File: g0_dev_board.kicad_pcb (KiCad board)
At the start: 4 copper layers, 80 x 114 mm, 198 parts, among them J201 USB_B_Mini, J202 F103_SWD, J301 USB_B_Mini, J401 RJ45_Hanrun_HR911105A_Horizon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, J501 DM3AT-SF-PEJM5, J801 Uno_IOH, J802 Uno_IOL, J803 Uno_POWER, J804 Uno_ANALOG, J805 J_LA_L, J806 J_LA_R, Q201 MMBT3904, SW701 RESET, SW702 USER, U101 STM32G0B1CCT6, U201 USBLC6-2SC6, U202 AP7361C-33E, U203 STM32F103CBTx, U301 USBLC6-2SC6, U302 FT232RL, U401 W5500, U501 W25Q32JVSSIQ, U601 TMP100, U602 TMP100, Y101 32.768kHz CL7pF, Y201 8MHz, Y401 25MHz

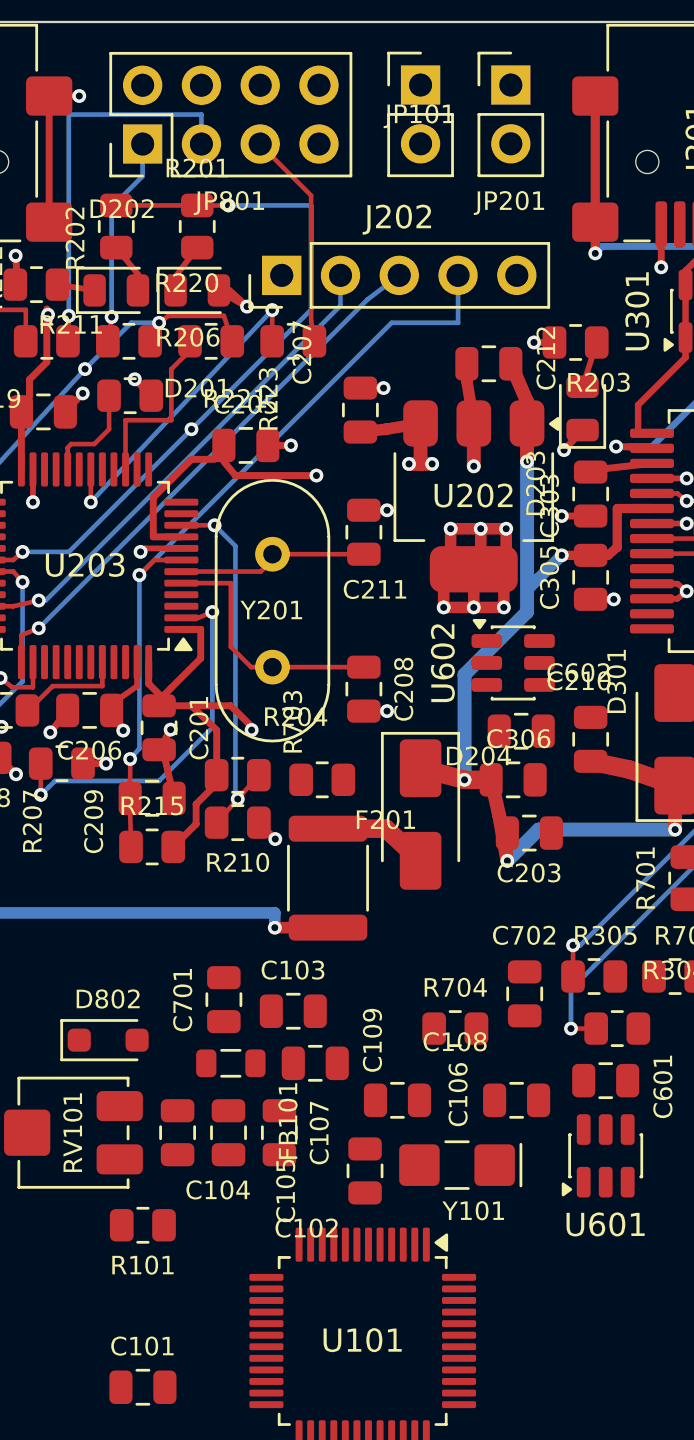
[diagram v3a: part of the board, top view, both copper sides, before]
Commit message: feat(pcb): route MCU top side, LSE crystal and +3V3_MCU feed
Кварц 32 кГц, VREF+ (FB101/C107/C109), развязка C102 (повёрнут, GND
вывода 7 напрямую), магистраль +3V3_MCU от JP101 (F.Cu -> B.Cu по
x=134.25) с ветками к C102 и к группе FB101/C104/C105/RV101. Выводы
BTN/PF0/PF1 выведены переходными внутрь корпуса. DRC: 0 ошибок.
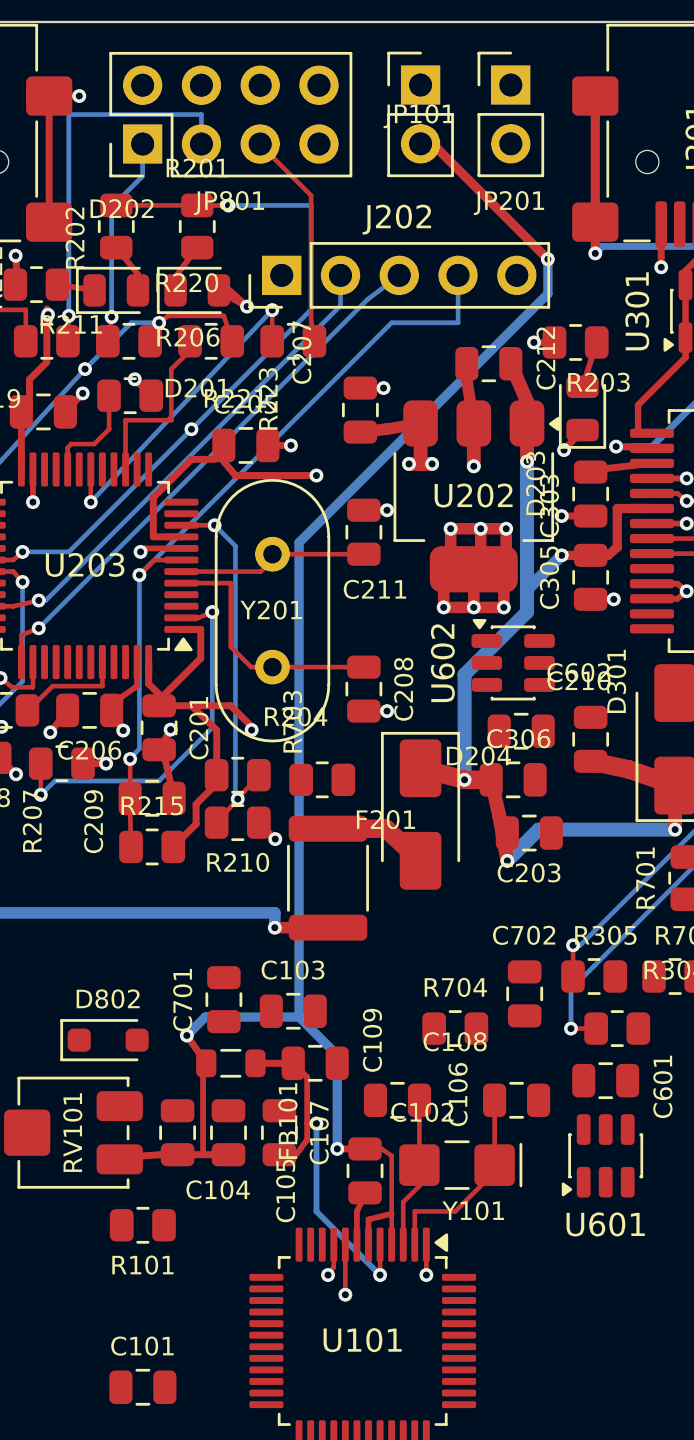
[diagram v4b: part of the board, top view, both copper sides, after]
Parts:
- turned C102 to -90 degrees
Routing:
- net +3V3_MCU: track 0.00 -> 73.9 mm, vias 0 -> 3
- net /VREF+: track 0.00 -> 15.4 mm, vias 0 -> 2
- net /cpu/OSC32_IN: track 0.00 -> 8.69 mm
- net /cpu/OSC32_OUT: track 0.00 -> 6.53 mm
- net /GPIO_PF0: track 0.00 -> 2.16 mm, vias 0 -> 1
- net GND: track 74.5 -> 76.5 mm
- net /GPIO_PF1: track 0.00 -> 1.39 mm, vias 0 -> 1
- net /BTN: track 0.00 -> 1.31 mm, vias 0 -> 1

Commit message: feat(pcb): route MCU right-side fanout to Uno and logic headers
Разведены 23 цепи правой стороны U101: D0-D13, U1_TX/U1_RX, SPI2,
W_INT, W_CS, I2C1 к J802/J803 и гребёнке J806, диагонали J80x-J806
и J804-J805, AREF. R801 повёрнут на 180 градусов для прохода AREF.
DRC: новых нарушений нет, неразведённых 267.
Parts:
- turned R801 to 180 degrees
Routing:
- net /D0: track 0.00 -> 68.9 mm, vias 0 -> 2
- net /D1: track 0.00 -> 67.7 mm, vias 0 -> 2
- net /D2: track 0.00 -> 65.1 mm, vias 0 -> 2
- net /D3: track 0.00 -> 63.8 mm, vias 0 -> 2
- net /D6: track 0.00 -> 59.6 mm, vias 0 -> 2
- net /W_CS: track 0.00 -> 57.8 mm, vias 0 -> 4
- net /D5: track 0.00 -> 57.1 mm, vias 0 -> 2
- net /D9: track 0.00 -> 54.4 mm, vias 0 -> 2
- net /D4: track 0.00 -> 54.1 mm, vias 0 -> 2
- net /U1_RX: track 0.00 -> 52.5 mm, vias 0 -> 2
- net /I2C1_SCL: track 0.00 -> 52.4 mm
- net /I2C1_SDA: track 0.00 -> 51.9 mm, vias 0 -> 2
- net /D7: track 0.00 -> 51.8 mm, vias 0 -> 2
- net /SPI2_MOSI: track 0.00 -> 51.4 mm, vias 0 -> 4
- net /U1_TX: track 0.00 -> 51.1 mm
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
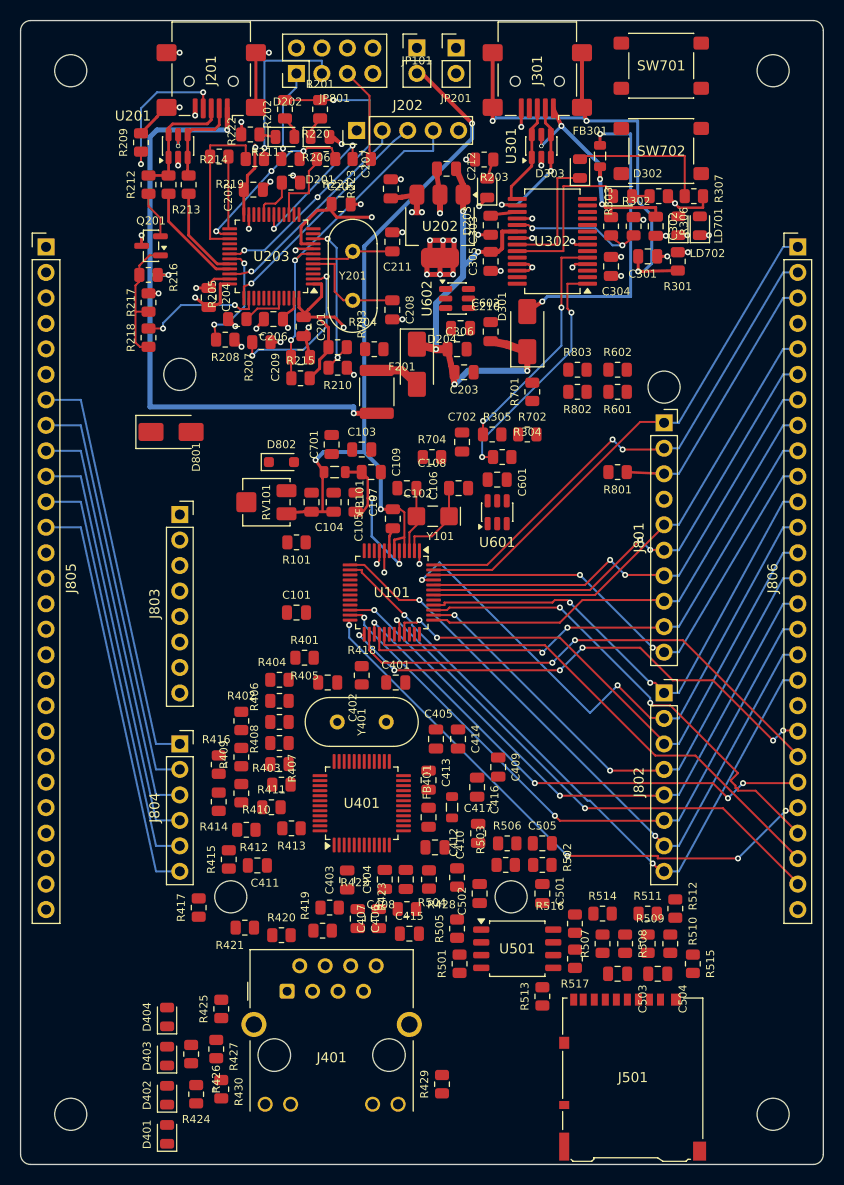
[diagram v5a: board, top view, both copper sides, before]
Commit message: refactor(pcb): reset routing, add power pins to J806, use GND on both inner layers
Плата откатена до расстановки: удалены все дорожки, переходные и полигоны.
Оба внутренних слоя (In1, In2) - сплошная общая GND.
Зафиксированы только контур платы, разъёмы Uno J801-J804, гребёнки
J805/J806 и крепёжные отверстия; остальные компоненты разблокированы
и оставлены на своих местах для ручной трассировки.

Схема: на гребёнке J806 вывод 3 (был AREF) -> +3.3V, вывод 27 (был GND)
-> +5V. Теперь на обеих гребёнках есть GND, +3.3V и +5V. AREF остаётся
только на разъёме Uno J801. ERC 0, DRC с паритетом схемы - 0 расхождений.
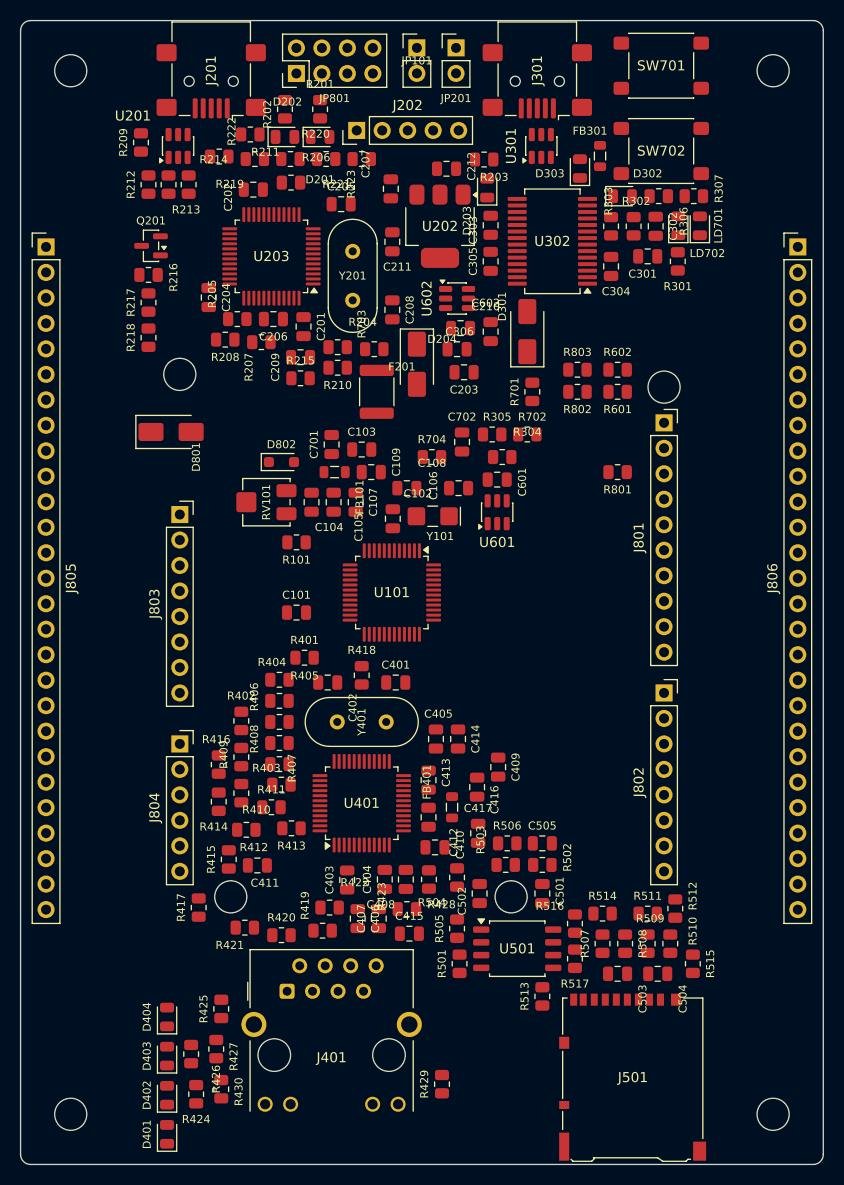
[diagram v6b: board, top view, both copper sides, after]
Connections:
- J806 pad 27: GND -> +5V
- J806 pad 3: /headers/AREF -> +3.3V
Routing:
- net GND: track 76.5 -> 0.00 mm, vias 45 -> 0
- net +3V3_MCU: track 73.9 -> 0.00 mm, vias 3 -> 0
- net /D0: track 68.9 -> 0.00 mm, vias 2 -> 0
- net /D1: track 67.7 -> 0.00 mm, vias 2 -> 0
- net /st_link/VBUS_STL: track 66.0 -> 0.00 mm, vias 4 -> 0
- net /D2: track 65.1 -> 0.00 mm, vias 2 -> 0
- net /D3: track 63.8 -> 0.00 mm, vias 2 -> 0
- net /D6: track 59.6 -> 0.00 mm, vias 2 -> 0
- net /W_CS: track 57.8 -> 0.00 mm, vias 4 -> 0
- net /D5: track 57.1 -> 0.00 mm, vias 2 -> 0
- net /D9: track 54.4 -> 0.00 mm, vias 2 -> 0
- net /D4: track 54.1 -> 0.00 mm, vias 2 -> 0
- net /U1_RX: track 52.5 -> 0.00 mm, vias 2 -> 0
- net /I2C1_SCL: track 52.4 -> 0.00 mm
- net /I2C1_SDA: track 51.9 -> 0.00 mm, vias 2 -> 0
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- added copper zone on In2.Cu, net GND
- removed copper zone on In2.Cu, net +3.3V
- removed copper zone on In2.Cu, net +3V3_STL
